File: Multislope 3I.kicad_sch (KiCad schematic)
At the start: 115 parts, among them J1 INT, J10 SLOT, J11 TEST, J12 UART, J13 INPUT, J2 TEST, J3 SLOT, J4 SLOT, J5 SLOT, J6 SLOT, J7 SLOT, J8 SLOT, J9 SLOT, Q1 5551, U1 OPA21xx, U10 LM311, U11 NE5534, U12 OPA197, U13 431, U14 431, U15 MCP3202, U16 Pico, U17 LM35, U18 ADuM121N, U2 LM399, U3 CD4053B, U4 OPA1xx, U5 OPA1xx, U6 OPA1xx, U7 431, U8 431, U9 408

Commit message: PCB compact-ified
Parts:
- removed J1: INT, Connector_PinHeader_2.54mm:PinHeader_1x03_P2.54mm_Vertical, symbol Connector_Generic:Conn_01x03
- removed J10, J3, J7, J8: SLOT, Connector_PinHeader_2.54mm:PinHeader_1x01_P2.54mm_Vertical, symbol Connector_Generic:Conn_01x01
- added H1, H2, H3, H4: MountingHole, MountingHole:MountingHole_3.2mm_M3_Pad_Via, symbol Mechanical:MountingHole
- added J1: INT, Connector_PinHeader_2.54mm:PinHeader_1x02_P2.54mm_Vertical, symbol Connector_Generic:Conn_01x02
- added J14: SLOPE, Connector_PinHeader_2.54mm:PinHeader_1x02_P2.54mm_Vertical, symbol Connector_Generic:Conn_01x02
- added J3: COMP, Connector_PinHeader_2.54mm:PinHeader_1x02_P2.54mm_Vertical, symbol Connector_Generic:Conn_01x02
- added J7: SLOPE2, Connector_PinHeader_2.54mm:PinHeader_1x02_P2.54mm_Vertical, symbol Connector_Generic:Conn_01x02
- R44: value 5K -> 50K
- R45: value 2K5 -> 25K
- R47: value 1K5 -> 15K
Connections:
- net GND: now also J1.2 (Pin_2), J14.2 (Pin_2), J3.2 (Pin_2), J7.2 (Pin_2)
- net INT: now also J1.1 (Pin_1)
- net COMP: now reaches R34.2, R35.1, U10.7, U16.12 (GPIO9)
- net COMP: now also J3.1 (Pin_1)
- net SLOPE: now reaches D1.2 (A), D2.1 (K), U10.3 (-), U11.6
- net SLOPE: now also J14.1 (Pin_1)
- net at J2.4 (Pin_4), R32.2: now also U16.2 (GPIO1); no longer U16.4 (GPIO2)
- net SLOPE2: now reaches R47.2, U12.6, U15.2 (CH0)
- net SLOPE2: now also J7.1 (Pin_1)
- net at J2.2 (Pin_2), R31.2: now also U16.4 (GPIO2); no longer U16.2 (GPIO1)
- no-connect marks 13 -> 12
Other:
- moved on the sheet: J11, J4, J5, J6, J9, N1

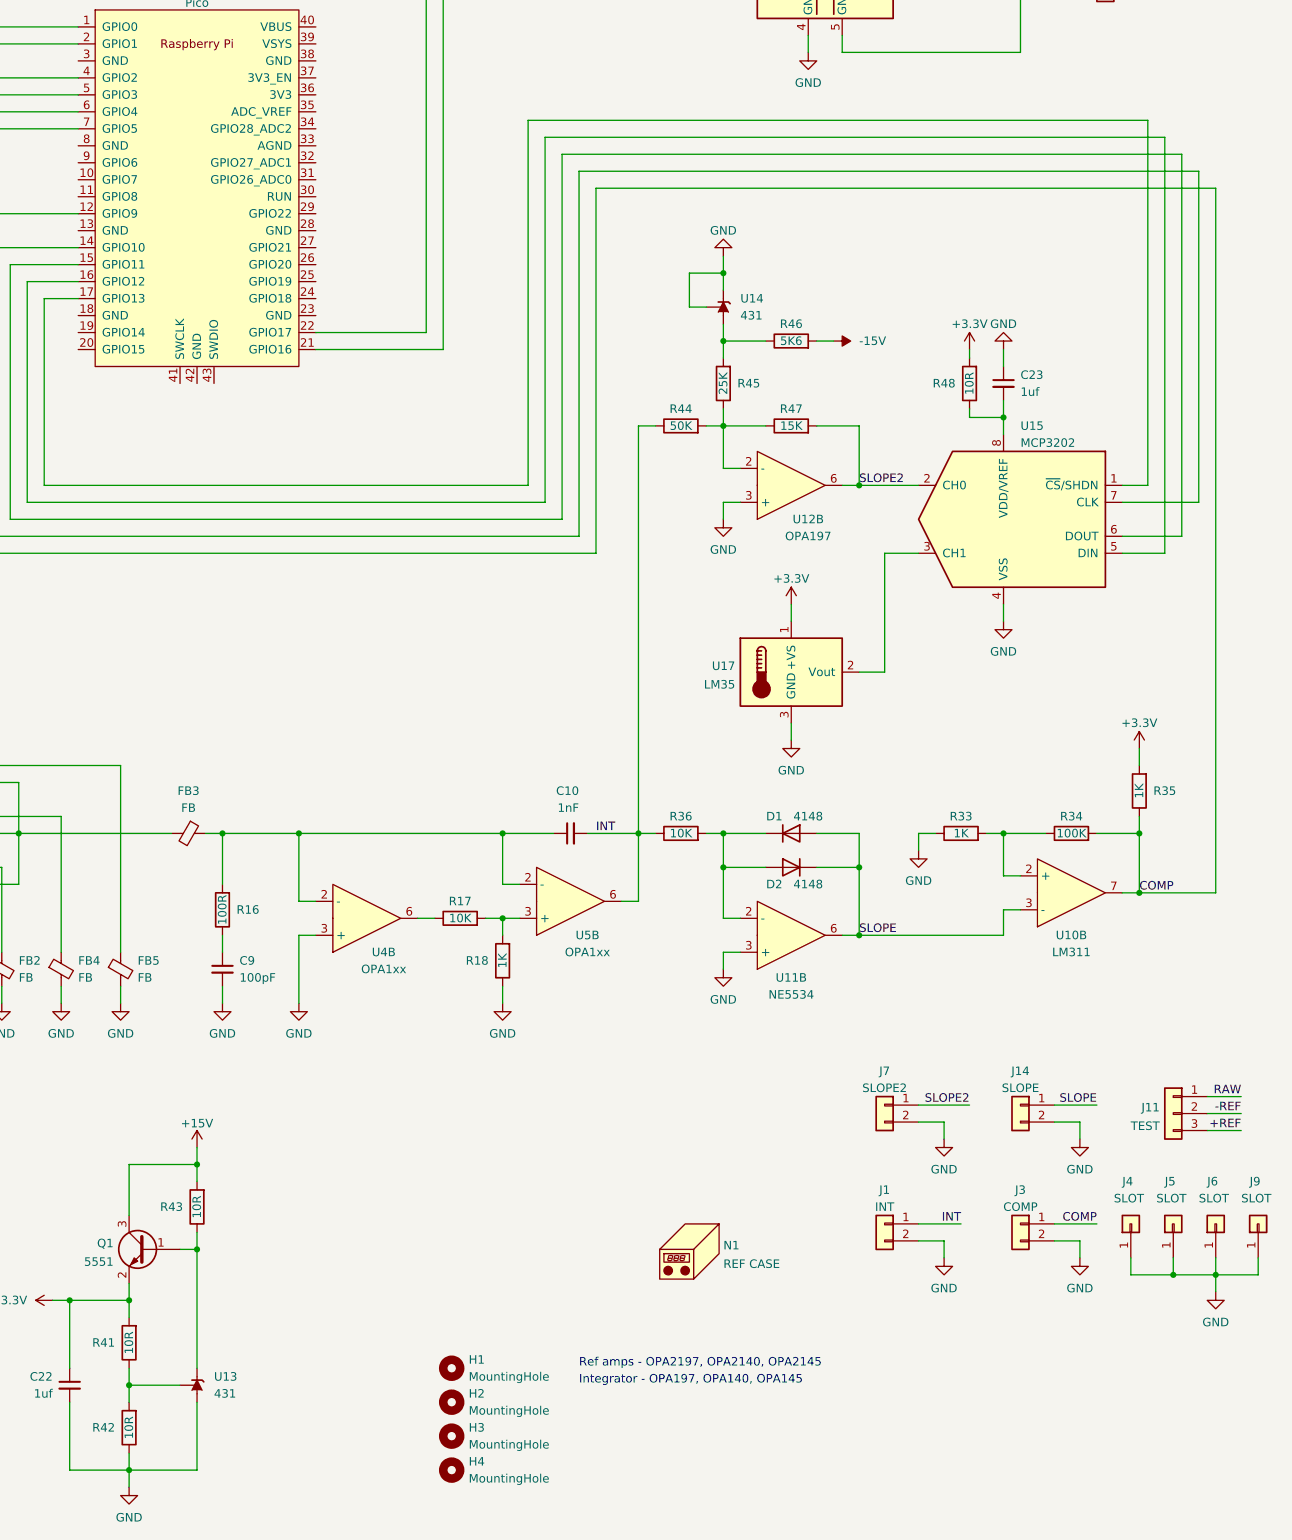
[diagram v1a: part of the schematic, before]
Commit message: removed redundant files
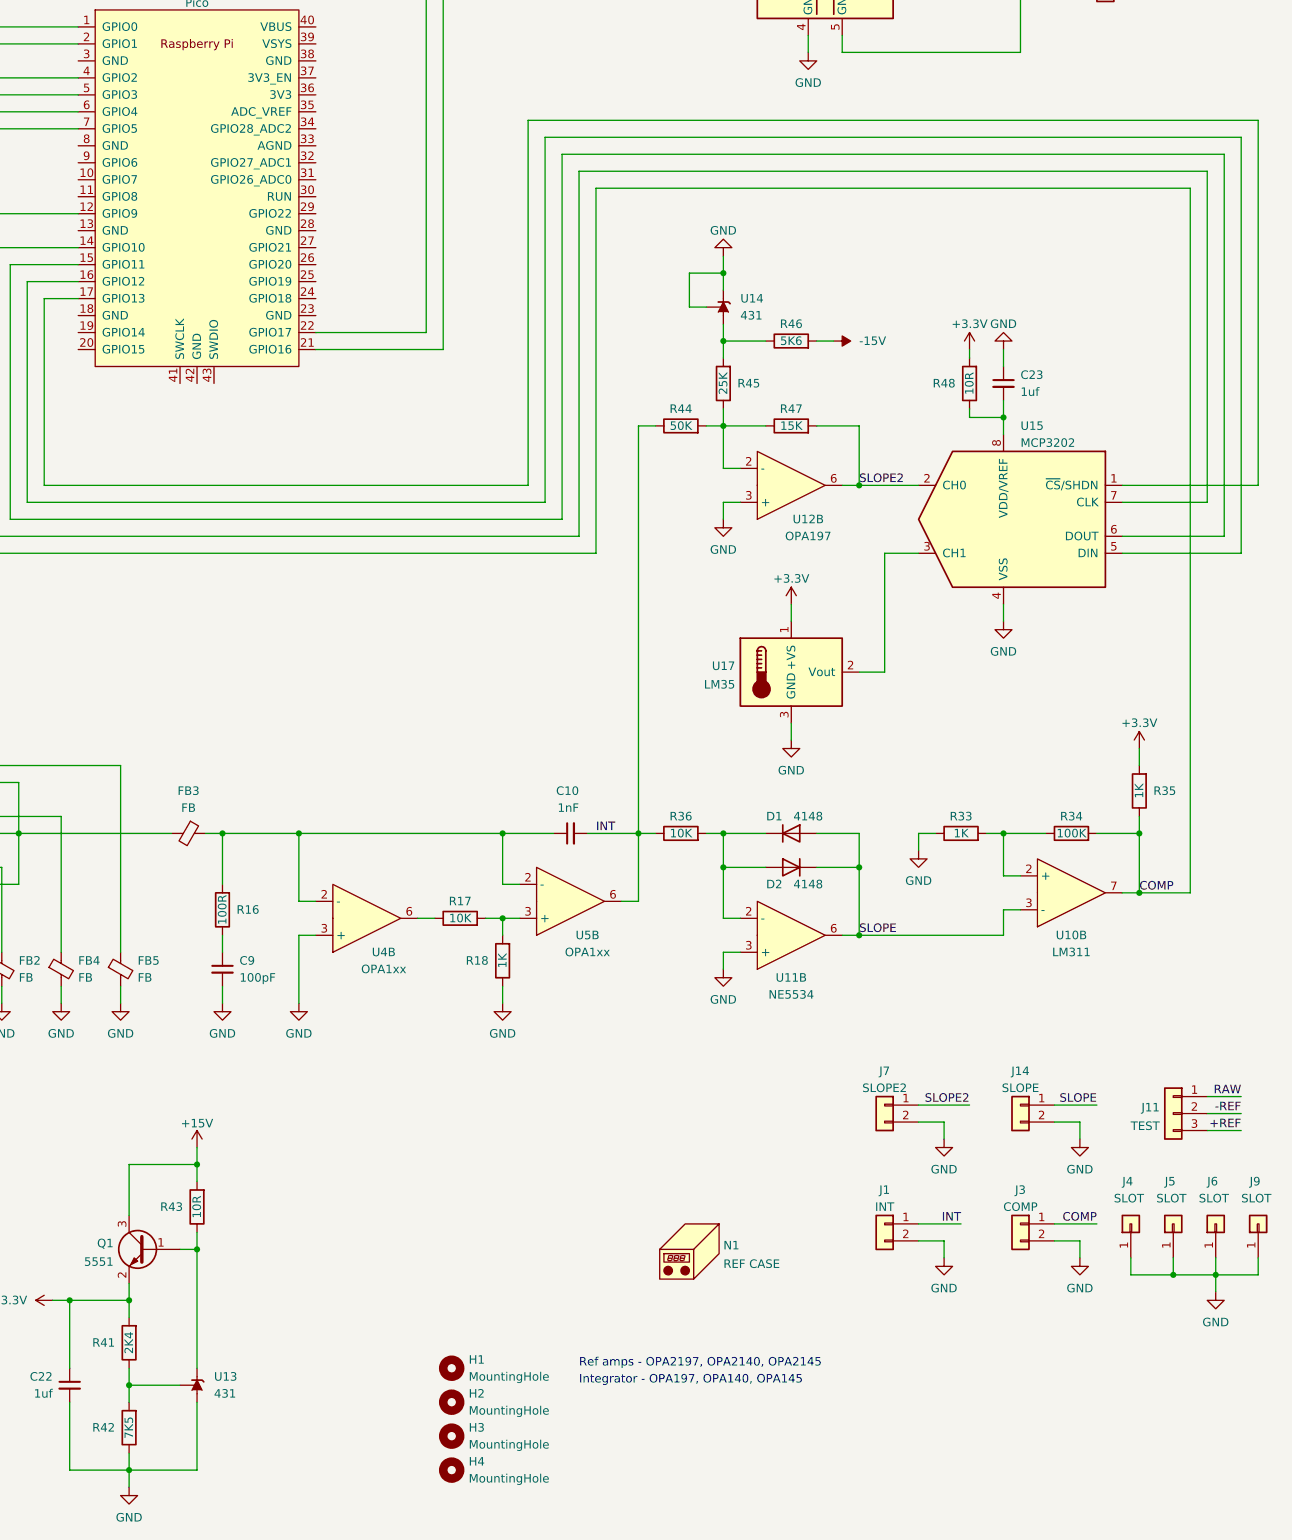
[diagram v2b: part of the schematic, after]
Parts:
- R41: value 10R -> 2K4
- R42: value 10R -> 7K5
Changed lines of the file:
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@@
     (stroke (width 0) (type default) (color 0 0 0 0))
   )
-  (wire (pts (xy 396.24 185.42) (xy 396.24 80.01))
+  (wire (pts (xy 392.43 185.42) (xy 392.43 80.01))
     (stroke (width 0) (type default) (color 0 0 0 0))
   )
@@
     (stroke (width 0) (type default) (color 0 0 0 0))
   )
-  (wire (pts (xy 396.24 80.01) (xy 303.53 80.01))
+  (wire (pts (xy 392.43 80.01) (xy 303.53 80.01))
     (stroke (width 0) (type default) (color 0 0 0 0))
   )
@@
     (stroke (width 0) (type default) (color 0 0 0 0))
   )
-  (wire (pts (xy 393.7 77.47) (xy 300.99 77.47))
+  (wire (pts (xy 394.97 77.47) (xy 300.99 77.47))
     (stroke (width 0) (type default) (color 0 0 0 0))
   )
@@
     (stroke (width 0) (type default) (color 0 0 0 0))
   )
-  (wire (pts (xy 382.27 124.46) (xy 386.08 124.46))
+  (wire (pts (xy 382.27 124.46) (xy 402.59 124.46))
     (stroke (width 0) (type default) (color 0 0 0 0))
   )
@@
     (stroke (width 0) (type default) (color 0 0 0 0))
   )
-  (wire (pts (xy 391.16 74.93) (xy 298.45 74.93))
+  (wire (pts (xy 397.51 74.93) (xy 298.45 74.93))
     (stroke (width 0) (type default) (color 0 0 0 0))
   )
@@
     (stroke (width 0) (type default) (color 0 0 0 0))
   )
-  (wire (pts (xy 391.16 132.08) (xy 391.16 74.93))
+  (wire (pts (xy 397.51 132.08) (xy 397.51 74.93))
     (stroke (width 0) (type default) (color 0 0 0 0))
   )
@@
     (stroke (width 0) (type default) (color 0 0 0 0))
   )
-  (wire (pts (xy 386.08 69.85) (xy 293.37 69.85))
+  (wire (pts (xy 402.59 69.85) (xy 293.37 69.85))
     (stroke (width 0) (type default) (color 0 0 0 0))
   )
@@
     (stroke (width 0) (type default) (color 0 0 0 0))
   )
-  (wire (pts (xy 382.27 127) (xy 393.7 127))
+  (wire (pts (xy 382.27 127) (xy 394.97 127))
     (stroke (width 0) (type default) (color 0 0 0 0))
   )
@@
     (stroke (width 0) (type default) (color 0 0 0 0))
   )
-  (wire (pts (xy 384.81 185.42) (xy 396.24 185.42))
+  (wire (pts (xy 384.81 185.42) (xy 392.43 185.42))
     (stroke (width 0) (type default) (color 0 0 0 0))
   )
@@
     (stroke (width 0) (type default) (color 0 0 0 0))
   )
-  (wire (pts (xy 382.27 132.08) (xy 391.16 132.08))
+  (wire (pts (xy 382.27 132.08) (xy 397.51 132.08))
     (stroke (width 0) (type default) (color 0 0 0 0))
   )
@@
     (stroke (width 0) (type default) (color 0 0 0 0))
   )
-  (wire (pts (xy 386.08 124.46) (xy 386.08 69.85))
+  (wire (pts (xy 402.59 124.46) (xy 402.59 69.85))
     (stroke (width 0) (type default) (color 0 0 0 0))
   )
@@
     (stroke (width 0) (type default) (color 0 0 0 0))
   )
-  (wire (pts (xy 388.62 72.39) (xy 388.62 134.62))
+  (wire (pts (xy 400.05 72.39) (xy 400.05 134.62))
     (stroke (width 0) (type default) (color 0 0 0 0))
   )
@@
     (stroke (width 0) (type default) (color 0 0 0 0))
   )
-  (wire (pts (xy 388.62 134.62) (xy 382.27 134.62))
+  (wire (pts (xy 400.05 134.62) (xy 382.27 134.62))
     (stroke (width 0) (type default) (color 0 0 0 0))
   )
@@
     (stroke (width 0) (type default) (color 0 0 0 0))
   )
-  (wire (pts (xy 295.91 72.39) (xy 388.62 72.39))
+  (wire (pts (xy 295.91 72.39) (xy 400.05 72.39))
     (stroke (width 0) (type default) (color 0 0 0 0))
   )
@@
     (stroke (width 0) (type default) (color 0 0 0 0))
   )
-  (wire (pts (xy 393.7 127) (xy 393.7 77.47))
+  (wire (pts (xy 394.97 127) (xy 394.97 77.47))
     (stroke (width 0) (type default) (color 0 0 0 0))
   )
@@
     (in_bom yes) (on_board yes)
     (property "Reference" "R41" (id 0) (at 229.87 252.73 0))
-    (property "Value" "10R" (id 1) (at 233.68 252.73 90))
+    (property "Value" "2K4" (id 1) (at 233.68 252.73 90))
     (property "Footprint" "Resistor_SMD:R_0603_1608Metric" (id 2) (at 235.458 252.73 90)
       (effects (font (size 1.27 1.27)) hide)
@@
     (in_bom yes) (on_board yes)
     (property "Reference" "R42" (id 0) (at 229.87 265.43 0))
-    (property "Value" "10R" (id 1) (at 233.68 265.43 90))
+    (property "Value" "7K5" (id 1) (at 233.68 265.43 90))
     (property "Footprint" "Resistor_SMD:R_0603_1608Metric" (id 2) (at 235.458 265.43 90)
       (effects (font (size 1.27 1.27)) hide)
@@
     )
     (path "/54ee8cfe-28f2-424b-8629-e51e250fbf55"
-      (reference "R41") (unit 1) (value "10R") (footprint "Resistor_SMD:R_0603_1608Metric")
+      (reference "R41") (unit 1) (value "2K4") (footprint "Resistor_SMD:R_0603_1608Metric")
     )
     (path "/98c22f57-ae24-4d97-a640-5f82a3fc2afa"
-      (reference "R42") (unit 1) (value "10R") (footprint "Resistor_SMD:R_0603_1608Metric")
+      (reference "R42") (unit 1) (value "7K5") (footprint "Resistor_SMD:R_0603_1608Metric")
     )
     (path "/49657b69-0138-4ffe-a1b6-0c0668091997"

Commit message: pcb completed
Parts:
- added C26: 1uf, Resistor_SMD:R_0603_1608Metric, symbol Device:C_Small
- added J10: PWR, Connector_PinHeader_2.54mm:PinHeader_1x04_P2.54mm_Vertical, symbol Connector_Generic:Conn_01x04
- added J8: PWR, Connector_PinHeader_2.54mm:PinHeader_1x03_P2.54mm_Vertical, symbol Connector_Generic:Conn_01x03
- R43: value 10R -> 10K
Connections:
- net +15V: now also J10.1 (Pin_1)
- net +3V3: now also J10.3 (Pin_3)
- net -15V: now also J10.2 (Pin_2)
- net COMP: now also U16.9 (GPIO6); no longer U16.12 (GPIO9)
- net GND: now also U16.13 (GND), U16.18 (GND), U16.23 (GND), U16.28 (GND), U16.3 (GND), U16.33 (AGND), U16.38 (GND), U16.42 (GND), U16.8 (GND), J10.4 (Pin_4), J8.2 (Pin_2)
- net at R32.2, U16.2 (GPIO1): now also J2.2 (Pin_2); no longer J2.4 (Pin_4)
- net at U16.11 (GPIO8): now also U18.3 (VIB)
- net at U16.21 (GPIO16): no longer U18.3 (VIB)
- net at U18.2 (VOA): now also U16.12 (GPIO9); no longer U16.22 (GPIO17)
- net at R31.2, U16.4 (GPIO2): now also J2.4 (Pin_4); no longer J2.2 (Pin_2)
- net at J12.1 (Pin_1), U18.8 (VDD2): now also C26.1
- net at J12.4 (Pin_4), U18.5 (GND2): now also C26.2
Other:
- moved on the sheet: U16

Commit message: 'final' PCB
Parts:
- added C27: 1uf, Resistor_SMD:R_0603_1608Metric, symbol Device:C_Small
- added Q2: 5551, Package_TO_SOT_SMD:SOT-23, symbol Transistor_BJT:MMBT5551L
- added R50, R51, R52: 10K, Resistor_SMD:R_0603_1608Metric, symbol Device:R
- added U19: 431, Package_TO_SOT_SMD:SOT-23, symbol Reference_Voltage:CJ432
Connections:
- net +15V: now also Q2.3 (C), R52.2
- net GND: now also C27.2, R51.1, U19.3 (A)
- net +5V: now reaches U16.39 (VSYS)
- net +5V: now also C27.1, Q2.2 (E), R50.2
- new net: Q2.1 (B), R52.1, U19.2 (K)
- new net: R50.1, R51.2, U19.1 (REF)
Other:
- moved on the sheet: C1, C14, C15, C16, C17, C18, C19, C20, C21, C22, C4, C5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

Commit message: minor mistakes fixed
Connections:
- net +15V: now also J8.1 (Pin_1)
- net +3V3: now also U9.2 (EN)
- net -15V: now also J8.3 (Pin_3)
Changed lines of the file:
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@@
     (stroke (width 0) (type default) (color 0 0 0 0))
   )
+  (wire (pts (xy 57.15 162.56) (xy 59.69 162.56))
+    (stroke (width 0) (type default) (color 0 0 0 0))
+  )
   (wire (pts (xy 269.24 60.96) (xy 269.24 73.66))
     (stroke (width 0) (type default) (color 0 0 0 0))
@@
     (pin "3")
   )
+  (symbol (lib_id "power:-15V") (at 331.47 222.25 270) (unit 1)
+    (in_bom yes) (on_board yes)
+    (property "Reference" "#PWR0118" (id 0) (at 334.01 222.25 0)
+      (effects (font (size 1.27 1.27)) hide)
+    )
+    (property "Value" "-15V" (id 1) (at 335.28 222.25 90)
+      (effects (font (size 1.27 1.27)) (justify left))
+    )
+    (property "Footprint" "" (id 2) (at 331.47 222.25 0)
+      (effects (font (size 1.27 1.27)) hide)
+    )
+    (property "Datasheet" "" (id 3) (at 331.47 222.25 0)
+      (effects (font (size 1.27 1.27)) hide)
+    )
+    (pin "1")
+  )
   (symbol (lib_id "Device:R") (at 384.81 170.18 180) (unit 1)
     (in_bom yes) (on_board yes)
@@
     (pin "1")
   )
+  (symbol (lib_id "power:+15V") (at 331.47 217.17 270) (unit 1)
+    (in_bom yes) (on_board yes)
+    (property "Reference" "#PWR0119" (id 0) (at 327.66 217.17 0)
+      (effects (font (size 1.27 1.27)) hide)
+    )
+    (property "Value" "+15V" (id 1) (at 335.28 217.17 90)
+      (effects (font (size 1.27 1.27)) (justify left))
+    )
+    (property "Footprint" "" (id 2) (at 331.47 217.17 0)
+      (effects (font (size 1.27 1.27)) hide)
+    )
+    (property "Datasheet" "" (id 3) (at 331.47 217.17 0)
+      (effects (font (size 1.27 1.27)) hide)
+    )
+    (pin "1")
+  )
   (symbol (lib_id "Device:FerriteBead_Small") (at 242.57 176.53 270) (unit 1)
     (in_bom yes) (on_board yes)
@@
     (pin "2")
   )
+  (symbol (lib_id "power:+3.3V") (at 57.15 162.56 90) (unit 1)
+    (in_bom yes) (on_board yes)
+    (property "Reference" "#PWR0117" (id 0) (at 60.96 162.56 0)
+      (effects (font (size 1.27 1.27)) hide)
+    )
+    (property "Value" "+3.3V" (id 1) (at 53.34 162.56 90)
+      (effects (font (size 1.27 1.27)) (justify left))
+    )
+    (property "Footprint" "" (id 2) (at 57.15 162.56 0)
+      (effects (font (size 1.27 1.27)) hide)
+    )
+    (property "Datasheet" "" (id 3) (at 57.15 162.56 0)
+      (effects (font (size 1.27 1.27)) hide)
+    )
+    (pin "1")
+  )
   (symbol (lib_id "Device:C_Small") (at 109.22 266.7 0) (unit 1)
     (in_bom yes) (on_board yes)
@@
       (reference "#PWR0116") (unit 1) (value "+5V") (footprint "")
     )
+    (path "/fe94c500-4723-4940-b5d8-70f2101badee"
+      (reference "#PWR0117") (unit 1) (value "+3.3V") (footprint "")
+    )
+    (path "/2531baad-8e8d-4d4c-bd98-5bc629cbfac5"
+      (reference "#PWR0118") (unit 1) (value "-15V") (footprint "")
+    )
+    (path "/a88ca92e-51b6-42c1-9553-54d7f23c5ea1"
+      (reference "#PWR0119") (unit 1) (value "+15V") (footprint "")
+    )
     (path "/6628b97a-bd0f-489d-8b60-169a53a549ac"

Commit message: pcb final touches
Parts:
- removed Q1, Q2: 5551, Package_TO_SOT_SMD:SOT-23, symbol Transistor_BJT:MMBT5551L
- removed R41: 2K4, Resistor_SMD:R_0603_1608Metric, symbol Device:R
- removed R42: 7K5, Resistor_SMD:R_0603_1608Metric, symbol Device:R
- removed R43, R50, R51, R52: 10K, Resistor_SMD:R_0603_1608Metric, symbol Device:R
- removed U13, U19: 431, Package_TO_SOT_SMD:SOT-23, symbol Reference_Voltage:CJ432
- added C28, C29, C30: 1uf, Resistor_SMD:R_0603_1608Metric, symbol Device:C_Small
- added J15: PWR, Connector_PinHeader_2.54mm:PinHeader_1x03_P2.54mm_Vertical, symbol Connector_Generic:Conn_01x03
- added SW1: RST, Button_Switch_SMD:SW_Push_1P1T_NO_CK_KMR2, symbol Switch:SW_SPST
- added U20: HT7533, Package_TO_SOT_SMD:SOT-89-3, symbol Regulator_Linear:HT75xx-1-SOT89
- added U21: HT7550, Package_TO_SOT_SMD:SOT-89-3, symbol Regulator_Linear:HT75xx-1-SOT89
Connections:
- net +15V: now also C22.1, C28.1, U20.2 (VIN), U21.2 (VIN)
- net +3V3: now also C27.1, C30.2, J15.1 (Pin_1), U20.3 (VOUT); no longer C22.1
- net +5V: now also C29.1, J15.2 (Pin_2), U21.3 (VOUT); no longer C27.1
- net GND: now also C28.2, C29.2, C30.1, J15.3 (Pin_3), SW1.1 (A), U20.1 (GND), U21.1 (GND)
- net at U16.30 (RUN): now also SW1.2 (B)
- no-connect marks 12 -> 31

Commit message: Changes
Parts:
- added R41, R42: 0R, 0603 Jumper:0603 Jumper, symbol Device:R
- R44: value 50K -> 51K
- R45: value 25K -> 24K
- R6, R7: value 0R -> 3K1
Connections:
- net SLOPE2: now also R41.1; no longer U15.2 (CH0)
- net PWMA: now reaches R27.1, U3.11 (S1)
- net PWMB: now reaches R28.1, U3.10 (S2)
- net at U16.15 (GPIO11): now also U15.5 (DIN); no longer U15.6 (DOUT)
- net at U16.16 (GPIO12): now also U15.6 (DOUT); no longer U15.5 (DIN)
- net at U17.2 (Vout): now also R42.1; no longer U15.3 (CH1)
- net MEAS: now reaches R29.1, U3.9 (S3)
- new net: R41.2, U15.2 (CH0)
- new net: R42.2, U15.3 (CH1)
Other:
- moved on the sheet: C23, R27, R28, R29, R48, U15
